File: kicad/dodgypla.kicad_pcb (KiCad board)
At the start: 2 copper layers, 19 x 36.8 mm, 8 parts, among them J1 PLA_Conn, J2 JTAG, U1 AMS1117, U2 XC9536XL

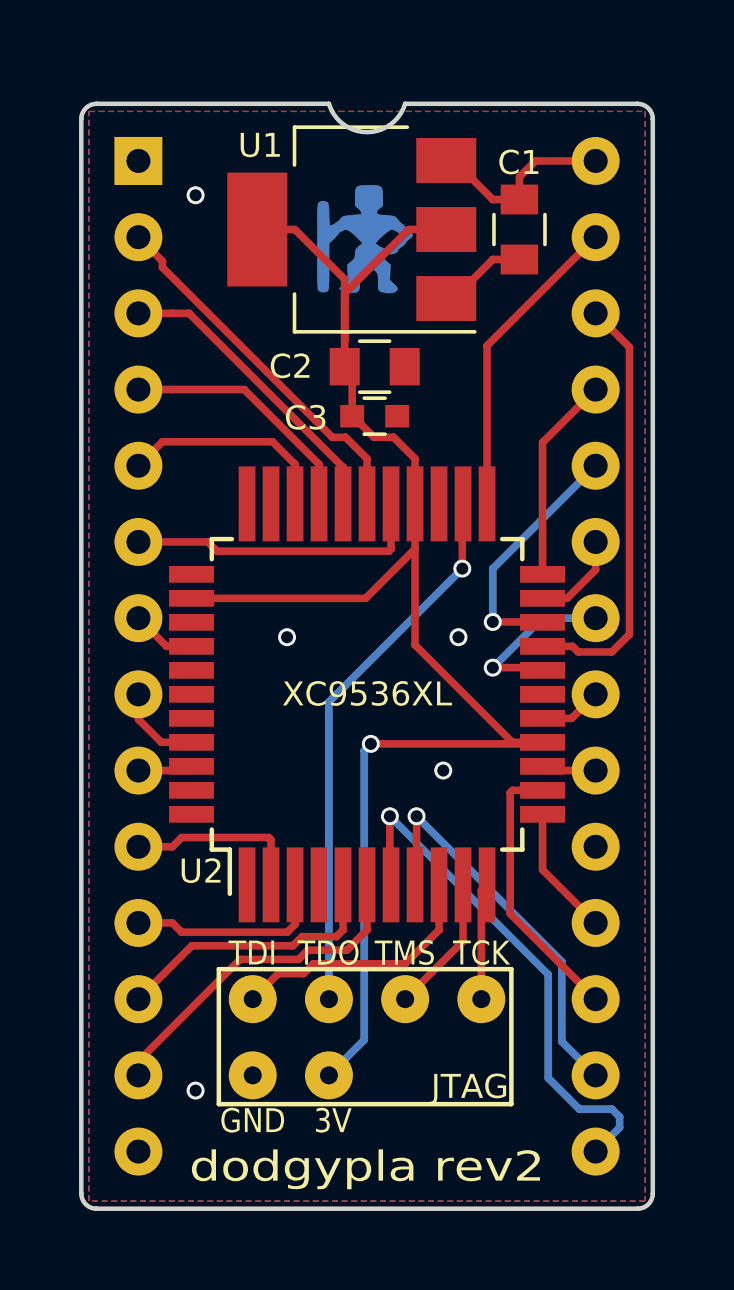
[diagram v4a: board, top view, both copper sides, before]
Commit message: Converting to two-layer board for PCB manufacturing.
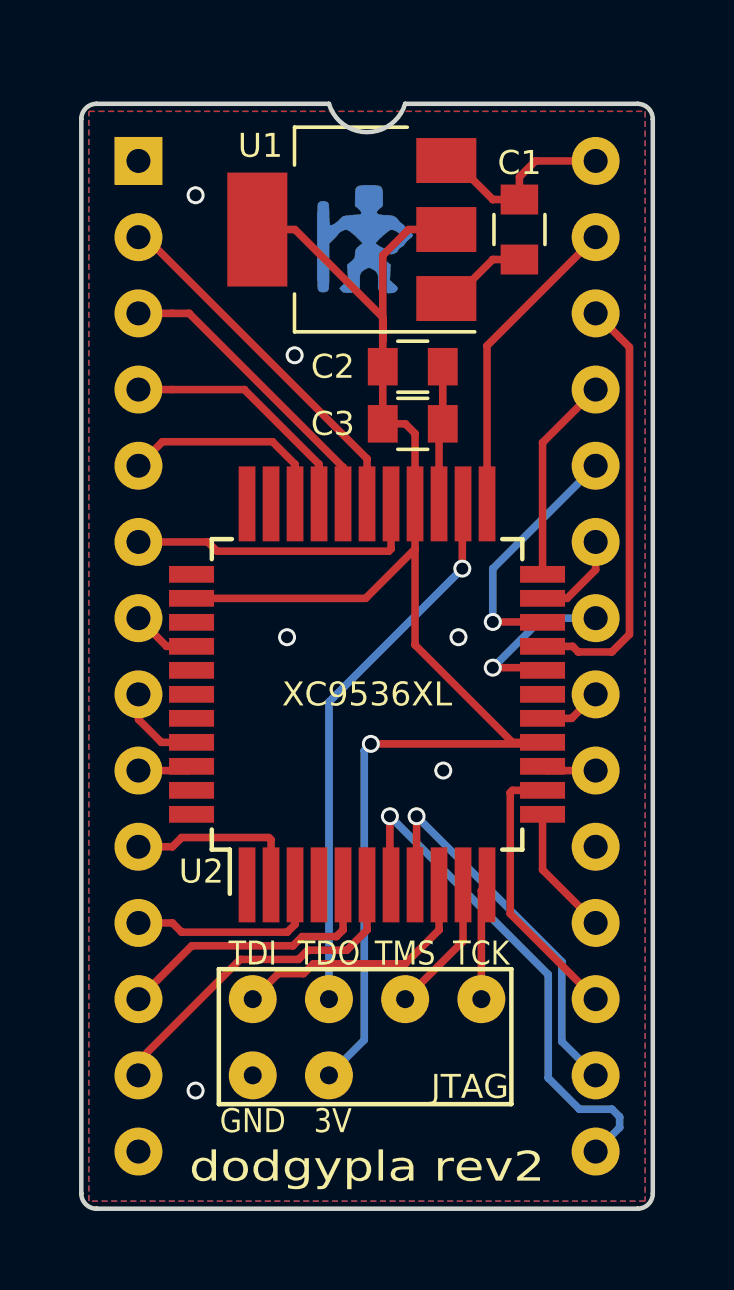
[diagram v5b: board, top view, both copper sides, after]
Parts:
- C3: footprint Capacitors_SMD:C_0603 -> Capacitors_SMD:C_0805
- moved C3 1.30 mm to (133.0, 89.7)
- moved C2 1.27 mm to (133.0, 87.8)
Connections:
- J1 pad 1: (no net) -> /PLA_FE
- J1 pad 19: (no net) -> /PLA_OE
- U2 pad 1: (no net) -> Net-(U2-Pad1)
- U2 pad 32: (no net) -> Net-(U2-Pad32)
- U2 pad 33: (no net) -> Net-(U2-Pad33)
- U2 pad 34: (no net) -> Net-(U2-Pad34)
- U2 pad 36: (no net) -> Net-(U2-Pad36)
- U2 pad 38: (no net) -> Net-(U2-Pad38)
- U2 pad 39: (no net) -> Net-(U2-Pad39)
- U2 pad 40: (no net) -> Net-(U2-Pad40)
- U2 pad 43: (no net) -> Net-(U2-Pad43)
- U2 pad 44: (no net) -> Net-(U2-Pad44)
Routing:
- net GND: track 2.98 -> 7.60 mm, vias 5 -> 6

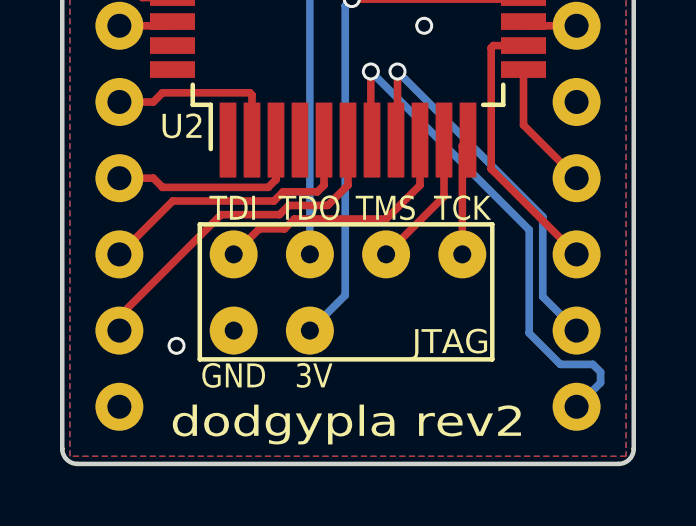
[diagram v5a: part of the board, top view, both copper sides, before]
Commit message: Converting to two-layer board for PCB manufacturing.
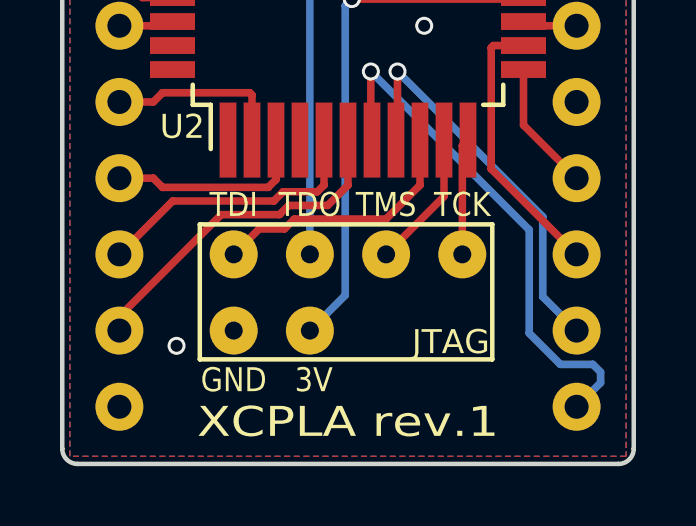
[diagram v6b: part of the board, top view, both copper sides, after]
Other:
- board text added: "XCPLA rev.1"
- board text removed: "dodgypla rev2"
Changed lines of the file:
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@@
     (effects (font (size 1 1) (thickness 0.15)) (justify left mirror))
   )
-  (gr_text GND (at 127.635 112.903) (layer F.SilkS)
+  (gr_text GND (at 127.635 113.03) (layer F.SilkS)
     (effects (font (size 0.8 0.7) (thickness 0.12)))
   )
-  (gr_text 3V (at 130.302 112.903) (layer F.SilkS)
+  (gr_text 3V (at 130.302 113.03) (layer F.SilkS)
     (effects (font (size 0.8 0.7) (thickness 0.12)))
   )
-  (gr_text TCK (at 135.255 107.315) (layer F.SilkS)
+  (gr_text TCK (at 135.255 107.188) (layer F.SilkS)
     (effects (font (size 0.8 0.7) (thickness 0.12)))
   )
-  (gr_text TMS (at 132.715 107.315) (layer F.SilkS)
+  (gr_text TMS (at 132.715 107.188) (layer F.SilkS)
     (effects (font (size 0.8 0.7) (thickness 0.12)))
   )
-  (gr_text TDO (at 130.175 107.315) (layer F.SilkS)
+  (gr_text TDO (at 130.175 107.188) (layer F.SilkS)
     (effects (font (size 0.8 0.7) (thickness 0.12)))
   )
-  (gr_text TDI (at 127.635 107.315) (layer F.SilkS)
+  (gr_text TDI (at 127.635 107.188) (layer F.SilkS)
     (effects (font (size 0.8 0.7) (thickness 0.12)))
   )
-  (gr_text "dodgypla rev2" (at 131.445 114.427) (layer F.SilkS)
+  (gr_text "XCPLA rev.1" (at 131.445 114.427) (layer F.SilkS)
     (effects (font (size 1 1.2) (thickness 0.2)))
   )

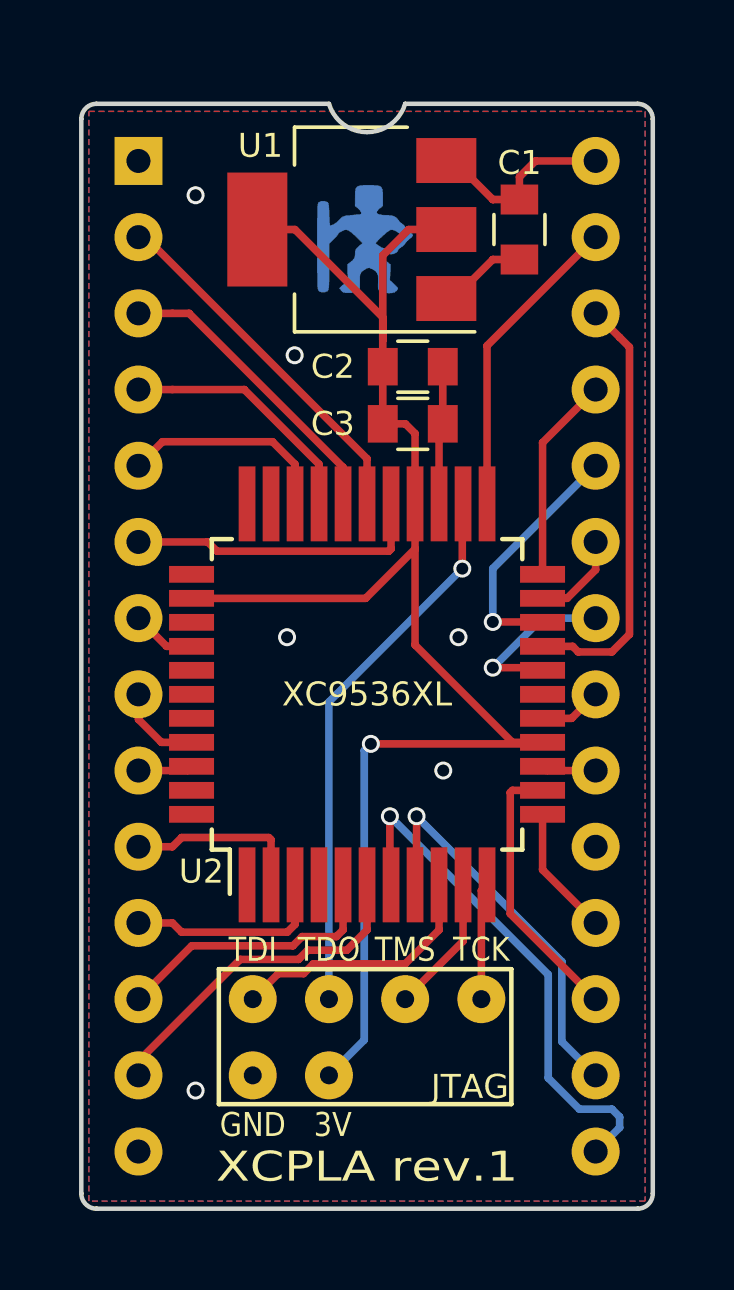
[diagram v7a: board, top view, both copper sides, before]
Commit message: Optimized JTAG header.
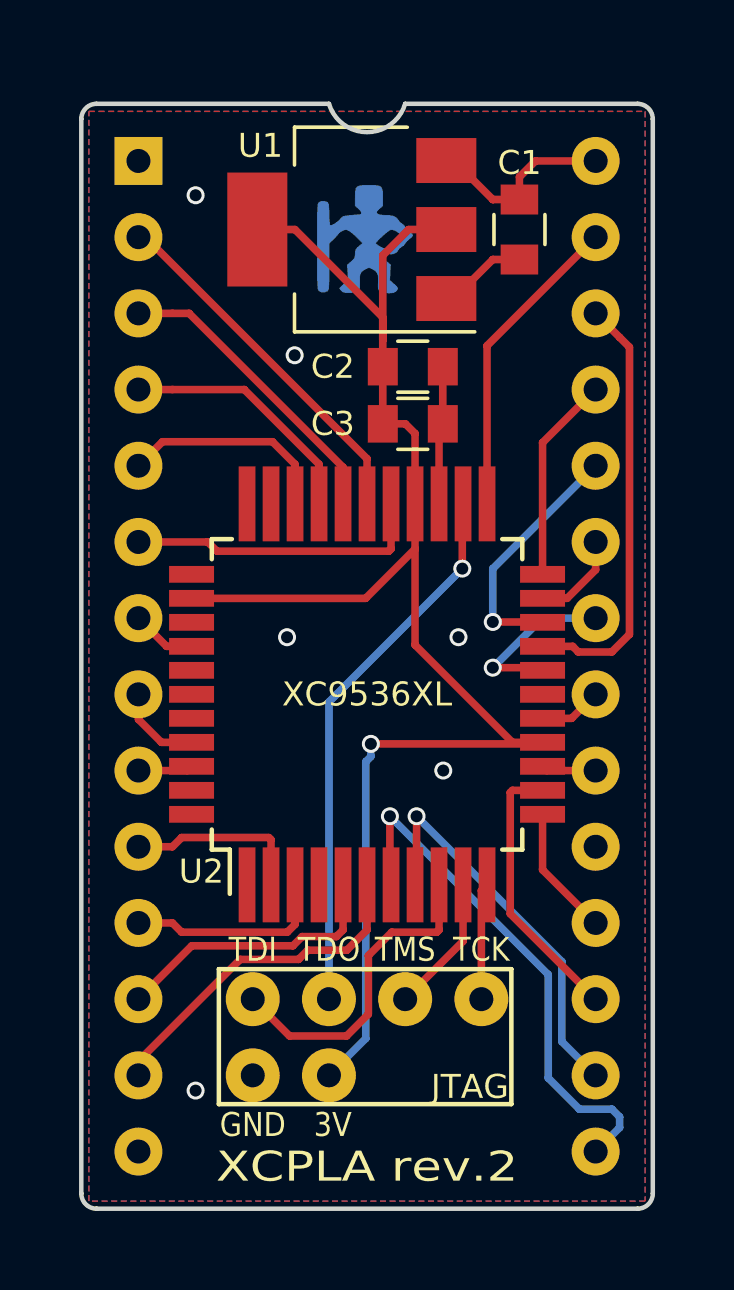
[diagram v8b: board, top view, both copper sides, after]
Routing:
- net /JTAG_TDI: track 8.67 -> 10.8 mm
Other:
- board text added: "XCPLA rev.2"
- board text removed: "XCPLA rev.1"
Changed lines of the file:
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@@
     (thickness 1.6)
     (drawings 18)
-    (tracks 159)
+    (tracks 162)
     (zones 0)
     (modules 8)
@@
   (title_block
     (title XCPLA)
-    (date 2019-05-31)
-    (rev 1)
+    (date 2019-06-04)
+    (rev 2)
     (company hackup.net)
     (comment 1 "Commodore 64 PLA Replacement")
@@
     (add_net "Net-(U2-Pad44)")
   )
+  (module Pin_Headers:Pin_Header_Straight_2x04_Pitch2.54mm (layer F.Cu)
+    (at 135.255 108.839 270)
+    (descr "Through hole straight pin header, 2x04, 2.54mm pitch, double rows")
+    (tags "Through hole pin header THT 2x04 2.54mm double row")
+    (fp_text reference J2 (at 1.27 -2.33 270) (layer F.SilkS) hide
+      (effects (font (size 1 1) (thickness 0.15)))
+    )
+    (fp_text value JTAG (at 2.921 0.381) (layer F.SilkS)
+      (effects (font (size 0.8 0.8) (thickness 0.12)))
+    )
+    (fp_line (start -1 8.75) (end 3.5 8.75) (layer F.SilkS) (width 0.15))
+    (fp_line (start -1 -1) (end -1 8.75) (layer F.SilkS) (width 0.15))
+    (fp_line (start 3.5 -1) (end -1 -1) (layer F.SilkS) (width 0.15))
+    (fp_line (start 3.5 8.75) (end 3.5 -1) (layer F.SilkS) (width 0.15))
+    (fp_text user %R (at 1.27 3.81) (layer F.Fab)
+      (effects (font (size 1 1) (thickness 0.15)))
+    )
+    (fp_line (start 4.35 -1.8) (end -1.8 -1.8) (layer F.CrtYd) (width 0.05))
+    (fp_line (start 4.35 9.4) (end 4.35 -1.8) (layer F.CrtYd) (width 0.05))
+    (fp_line (start -1.8 9.4) (end 4.35 9.4) (layer F.CrtYd) (width 0.05))
+    (fp_line (start -1.8 -1.8) (end -1.8 9.4) (layer F.CrtYd) (width 0.05))
+    (fp_line (start -1.27 0) (end 0 -1.27) (layer F.Fab) (width 0.1))
+    (fp_line (start -1.27 8.89) (end -1.27 0) (layer F.Fab) (width 0.1))
+    (fp_line (start 3.81 8.89) (end -1.27 8.89) (layer F.Fab) (width 0.1))
+    (fp_line (start 3.81 -1.27) (end 3.81 8.89) (layer F.Fab) (width 0.1))
+    (fp_line (start 0 -1.27) (end 3.81 -1.27) (layer F.Fab) (width 0.1))
+    (pad 8 thru_hole circle (at 2.54 7.62 270) (size 1.8 1.8) (drill 0.8) (layers *.Cu *.Mask)
+      (net 31 GND))
+    (pad 7 thru_hole circle (at 0 7.62 270) (size 1.8 1.8) (drill 0.8) (layers *.Cu *.Mask)
+      (net 30 /JTAG_TDI))
+    (pad 6 thru_hole circle (at 2.54 5.08 270) (size 1.8 1.8) (drill 0.8) (layers *.Cu *.Mask)
+      (net 2 +3V3))
+    (pad 5 thru_hole circle (at 0 5.08 270) (size 1.8 1.8) (drill 0.8) (layers *.Cu *.Mask)
+      (net 29 /JTAG_TDO))
+    (pad 3 thru_hole circle (at 0 2.54 270) (size 1.8 1.8) (drill 0.8) (layers *.Cu *.Mask)
+      (net 28 /JTAG_TMS))
+    (pad 1 thru_hole circle (at 0 0 270) (size 1.8 1.8) (drill 0.8) (layers *.Cu *.Mask)
+      (net 27 /JTAG_TCK))
+    (model ${KISYS3DMOD}/Pin_Headers.3dshapes/Pin_Header_Straight_2x04_Pitch2.54mm.wrl
+      (at (xyz 0 0 0))
+      (scale (xyz 1 1 1))
+      (rotate (xyz 0 0 0))
+    )
+  )
   (module Logo:bigby2 (layer B.Cu)
     (at 131.318 83.439 180)
@@
       (xy -0.537743 1.706143) (xy -0.434455 1.724827) (xy -0.281922 1.730119) (xy -0.1905 1.730375)
       (xy -0.011485 1.728467)) (layer B.Cu) (width 0.01))
-  )
-  (module Pin_Headers:Pin_Header_Straight_2x04_Pitch2.54mm (layer F.Cu)
-    (at 135.255 108.839 270)
-    (descr "Through hole straight pin header, 2x04, 2.54mm pitch, double rows")
-    (tags "Through hole pin header THT 2x04 2.54mm double row")
-    (fp_text reference J2 (at 1.27 -2.33 270) (layer F.SilkS) hide
-      (effects (font (size 1 1) (thickness 0.15)))
-    )
-    (fp_text value JTAG (at 2.921 0.381) (layer F.SilkS)
-      (effects (font (size 0.8 0.8) (thickness 0.12)))
-    )
-    (fp_line (start -1 8.75) (end 3.5 8.75) (layer F.SilkS) (width 0.15))
-    (fp_line (start -1 -1) (end -1 8.75) (layer F.SilkS) (width 0.15))
-    (fp_line (start 3.5 -1) (end -1 -1) (layer F.SilkS) (width 0.15))
-    (fp_line (start 3.5 8.75) (end 3.5 -1) (layer F.SilkS) (width 0.15))
-    (fp_text user %R (at 1.27 3.81) (layer F.Fab)
-      (effects (font (size 1 1) (thickness 0.15)))
-    )
-    (fp_line (start 4.35 -1.8) (end -1.8 -1.8) (layer F.CrtYd) (width 0.05))
-    (fp_line (start 4.35 9.4) (end 4.35 -1.8) (layer F.CrtYd) (width 0.05))
-    (fp_line (start -1.8 9.4) (end 4.35 9.4) (layer F.CrtYd) (width 0.05))
-    (fp_line (start -1.8 -1.8) (end -1.8 9.4) (layer F.CrtYd) (width 0.05))
-    (fp_line (start -1.27 0) (end 0 -1.27) (layer F.Fab) (width 0.1))
-    (fp_line (start -1.27 8.89) (end -1.27 0) (layer F.Fab) (width 0.1))
-    (fp_line (start 3.81 8.89) (end -1.27 8.89) (layer F.Fab) (width 0.1))
-    (fp_line (start 3.81 -1.27) (end 3.81 8.89) (layer F.Fab) (width 0.1))
-    (fp_line (start 0 -1.27) (end 3.81 -1.27) (layer F.Fab) (width 0.1))
-    (pad 8 thru_hole circle (at 2.54 7.62 270) (size 1.6 1.6) (drill 0.6) (layers *.Cu *.Mask)
-      (net 31 GND))
-    (pad 7 thru_hole circle (at 0 7.62 270) (size 1.6 1.6) (drill 0.6) (layers *.Cu *.Mask)
-      (net 30 /JTAG_TDI))
-    (pad 6 thru_hole circle (at 2.54 5.08 270) (size 1.6 1.6) (drill 0.6) (layers *.Cu *.Mask)
-      (net 2 +3V3))
-    (pad 5 thru_hole circle (at 0 5.08 270) (size 1.6 1.6) (drill 0.6) (layers *.Cu *.Mask)
-      (net 29 /JTAG_TDO))
-    (pad 3 thru_hole circle (at 0 2.54 270) (size 1.6 1.6) (drill 0.6) (layers *.Cu *.Mask)
-      (net 28 /JTAG_TMS))
-    (pad 1 thru_hole circle (at 0 0 270) (size 1.6 1.6) (drill 0.6) (layers *.Cu *.Mask)
-      (net 27 /JTAG_TCK))
-    (model ${KISYS3DMOD}/Pin_Headers.3dshapes/Pin_Header_Straight_2x04_Pitch2.54mm.wrl
-      (at (xyz 0 0 0))
-      (scale (xyz 1 1 1))
-      (rotate (xyz 0 0 0))
-    )
   )
   (module Housings_DIP:DIP-28_W15.24mm_Socket locked (layer F.Cu)
@@
     (effects (font (size 0.8 0.7) (thickness 0.12)))
   )
-  (gr_text "XCPLA rev.1" (at 131.445 114.427) (layer F.SilkS)
+  (gr_text "XCPLA rev.2" (at 131.445 114.427) (layer F.SilkS)
     (effects (font (size 1 1.2) (thickness 0.2)))
   )
@@
   (segment (start 136.291 100.279) (end 133.045 97.033) (width 0.254) (layer F.Cu) (net 2))
   (via (at 131.572 100.33) (size 0.6) (drill 0.4) (layers F.Cu B.Cu) (net 2))
-  (segment (start 131.352001 100.549999) (end 131.572 100.33) (width 0.254) (layer B.Cu) (net 2))
-  (segment (start 130.175 111.379) (end 131.352001 110.201999) (width 0.254) (layer B.Cu) (net 2))
-  (segment (start 131.352001 110.201999) (end 131.352001 100.549999) (width 0.254) (layer B.Cu) (net 2))
   (segment (start 137.244 100.33) (end 137.295 100.279) (width 0.254) (layer F.Cu) (net 2))
   (segment (start 131.572 100.33) (end 137.244 100.33) (width 0.254) (layer F.Cu) (net 2))
@@
   (segment (start 134.087 83.185) (end 132.833 83.185) (width 0.254) (layer F.Cu) (net 2))
   (segment (start 132.833 83.185) (end 131.969 84.049) (width 0.254) (layer F.Cu) (net 2))
+  (segment (start 131.572 100.754264) (end 131.572 100.33) (width 0.254) (layer B.Cu) (net 2))
+  (segment (start 131.402001 100.924263) (end 131.572 100.754264) (width 0.254) (layer B.Cu) (net 2))
+  (segment (start 130.175 111.379) (end 131.402001 110.151999) (width 0.254) (layer B.Cu) (net 2))
+  (segment (start 131.402001 110.151999) (end 131.402001 100.924263) (width 0.254) (layer B.Cu) (net 2))
   (segment (start 137.483989 108.019989) (end 132.207 102.743) (width 0.254) (layer B.Cu) (net 3))
   (segment (start 139.864999 113.119001) (end 139.864999 112.765039) (width 0.254) (layer B.Cu) (net 3))
@@
   (segment (start 130.175 98.933) (end 134.62 94.488) (width 0.254) (layer B.Cu) (net 29))
   (segment (start 130.175 108.839) (end 130.175 98.933) (width 0.254) (layer B.Cu) (net 29))
-  (segment (start 128.484999 107.989001) (end 129.329805 107.989001) (width 0.254) (layer F.Cu) (net 30))
-  (segment (start 129.329805 107.989001) (end 129.656807 107.661999) (width 0.254) (layer F.Cu) (net 30))
-  (segment (start 132.716001 107.661999) (end 133.845 106.533) (width 0.254) (layer F.Cu) (net 30))
-  (segment (start 129.656807 107.661999) (end 132.716001 107.661999) (width 0.254) (layer F.Cu) (net 30))
-  (segment (start 127.635 108.839) (end 128.484999 107.989001) (width 0.254) (layer F.Cu) (net 30))
   (segment (start 133.845 106.533) (end 133.845 105.029) (width 0.254) (layer F.Cu) (net 30))
+  (segment (start 133.771999 106.606001) (end 133.845 106.533) (width 0.254) (layer F.Cu) (net 30))
+  (segment (start 128.862001 110.066001) (end 130.763961 110.066001) (width 0.254) (layer F.Cu) (net 30))
+  (segment (start 127.635 108.839) (end 128.862001 110.066001) (width 0.254) (layer F.Cu) (net 30))
+  (segment (start 130.763961 110.066001) (end 131.487999 109.341963) (width 0.254) (layer F.Cu) (net 30))
+  (segment (start 131.487999 109.341963) (end 131.487999 107.386001) (width 0.254) (layer F.Cu) (net 30))
+  (segment (start 131.487999 107.386001) (end 132.267999 106.606001) (width 0.254) (layer F.Cu) (net 30))
+  (segment (start 132.267999 106.606001) (end 133.771999 106.606001) (width 0.254) (layer F.Cu) (net 30))
   (segment (start 135.646 84.185) (end 136.525 84.185) (width 0.254) (layer F.Cu) (net 31) (status 20))
   (segment (start 135.637 84.185) (end 135.646 84.185) (width 0.254) (layer F.Cu) (net 31))
